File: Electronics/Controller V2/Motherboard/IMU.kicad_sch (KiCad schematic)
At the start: 1 part, among them U3 Adafruit BNO085

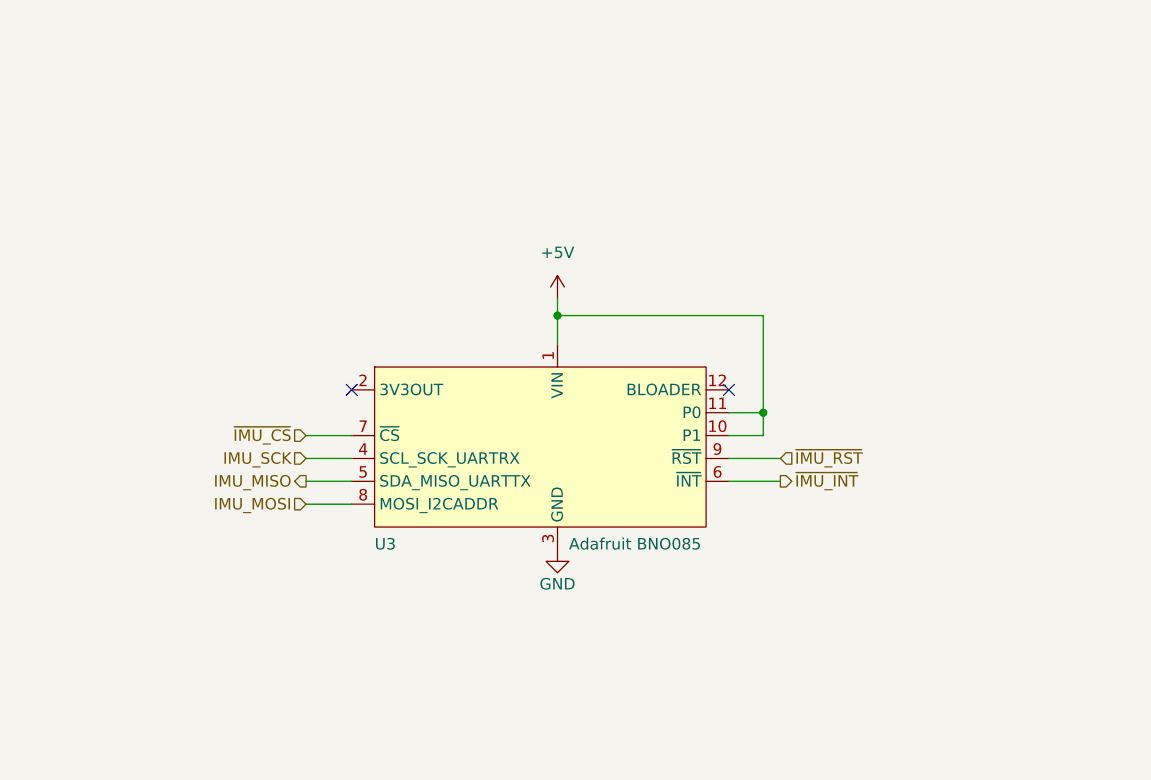
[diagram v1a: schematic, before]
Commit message: Added generic IMU option.
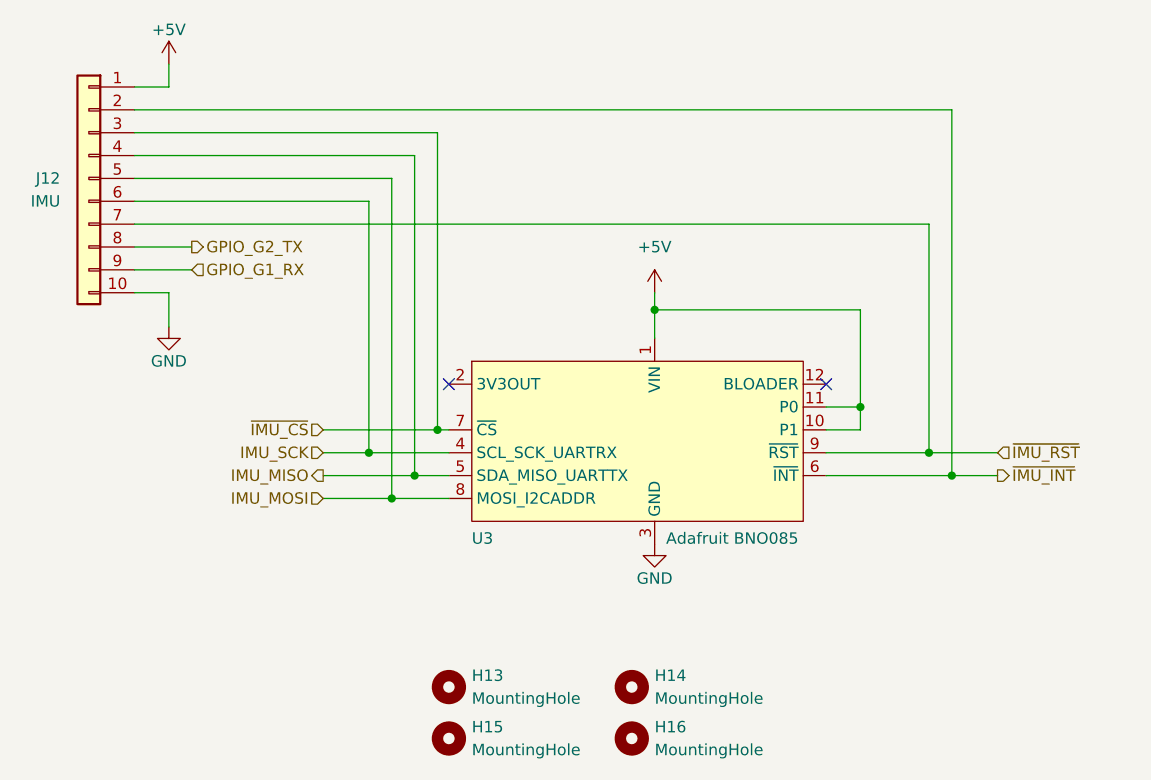
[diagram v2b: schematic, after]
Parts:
- added H13, H14, H15, H16: MountingHole, MountingHole:MountingHole_3.2mm_M3, symbol Mechanical:MountingHole
- added J12: IMU, Connector_JST:JST_PH_B10B-PH-K_1x10_P2.00mm_Vertical, symbol Connector_Generic:Conn_01x10
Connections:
- net +5V: now also J12.1 (Pin_1)
- net GND: now also J12.10 (Pin_10)
- net IMU_MISO: now also J12.4 (Pin_4)
- net IMU_MOSI: now also J12.5 (Pin_5)
- net IMU_SCK: now also J12.6 (Pin_6)
- net ~{IMU_CS}: now also J12.3 (Pin_3)
- net ~{IMU_INT}: now also J12.2 (Pin_2)
- net ~{IMU_RST}: now also J12.7 (Pin_7)
- new net GPIO_G1_RX: J12.9 (Pin_9)
- new net GPIO_G2_TX: J12.8 (Pin_8)
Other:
- moved on the sheet: U3

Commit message: Changed BMO085 from 5V to 3.3V to match Teensy.
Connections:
- net +5V: no longer U3.1 (VIN), U3.10 (P1), U3.11 (P0)
- new net +3V3: U3.1 (VIN), U3.10 (P1), U3.11 (P0)
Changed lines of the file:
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@@
     )
   )
-  (symbol (lib_id "power:+5V") (at 157.48 85.725 0) (unit 1)
-    (in_bom yes) (on_board yes) (dnp no) (fields_autoplaced)
+  (symbol (lib_id "power:+3V3") (at 157.48 85.725 0) (unit 1)
+    (in_bom yes) (on_board yes) (dnp no)
     (property "Reference" "#PWR09" (at 157.48 89.535 0)
       (effects (font (size 1.27 1.27)) hide)
     )
-    (property "Value" "+5V" (at 157.48 80.645 0)
+    (property "Value" "+3V3" (at 157.48 81.915 0)
       (effects (font (size 1.27 1.27)))
     )

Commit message: Added jumper to bypass current sensing. Minor tweaks. Generated production files.
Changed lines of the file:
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@@
     (effects (font (size 1.27 1.27)) (justify right))
   )
-  (hierarchical_label "GPIO_G1_RX" (shape input) (at 106.045 83.185 0) (fields_autoplaced)
+  (hierarchical_label "GPIO_G1_RX" (shape output) (at 106.045 83.185 0) (fields_autoplaced)
     (effects (font (size 1.27 1.27)) (justify left))
   )
-  (hierarchical_label "GPIO_G2_TX" (shape output) (at 106.045 80.645 0) (fields_autoplaced)
+  (hierarchical_label "GPIO_G2_TX" (shape input) (at 106.045 80.645 0) (fields_autoplaced)
     (effects (font (size 1.27 1.27)) (justify left))
   )
